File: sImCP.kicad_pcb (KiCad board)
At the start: 2 copper layers, 155.6 x 140 mm, 79 parts, among them J1 AVR-ISP-6, SW1 RESET, SW2 BOOT, U1 ATmega328P-AU, Y1 16MHz

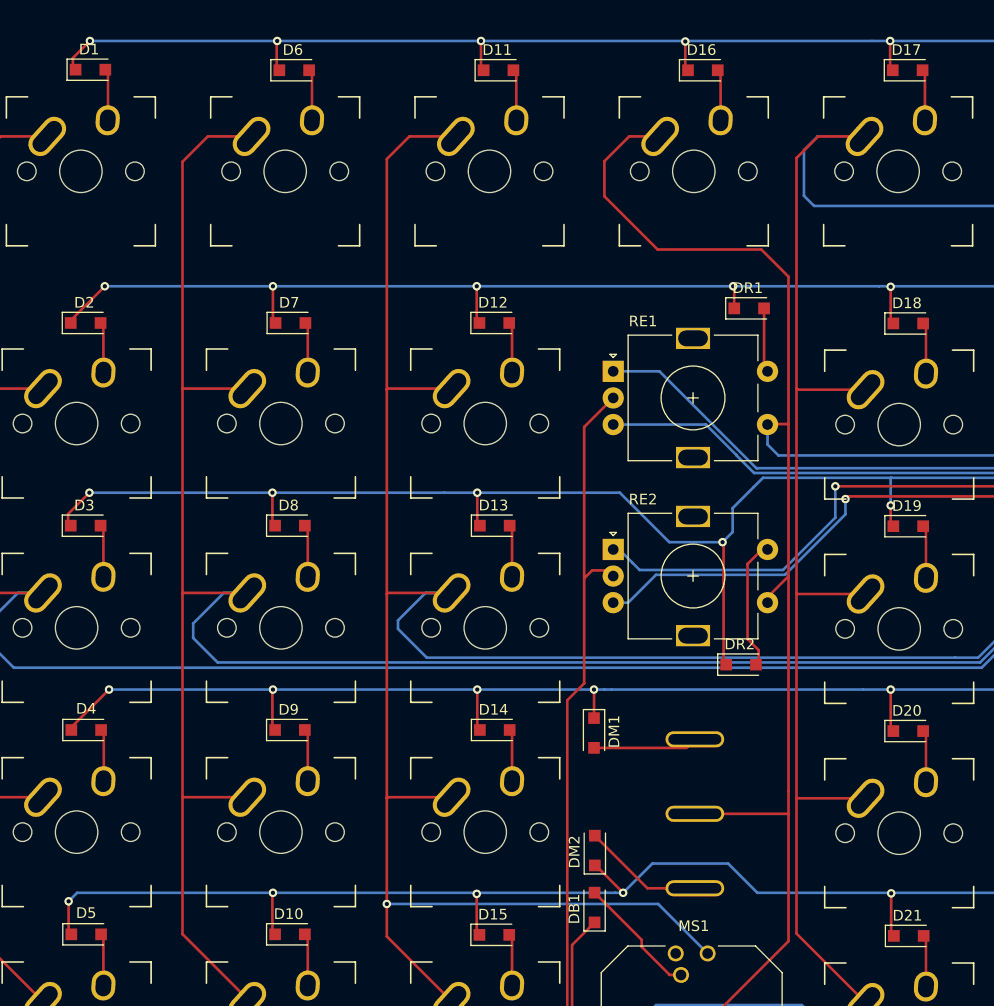
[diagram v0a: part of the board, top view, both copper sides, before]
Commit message: update diode footprint to SOD-123FL
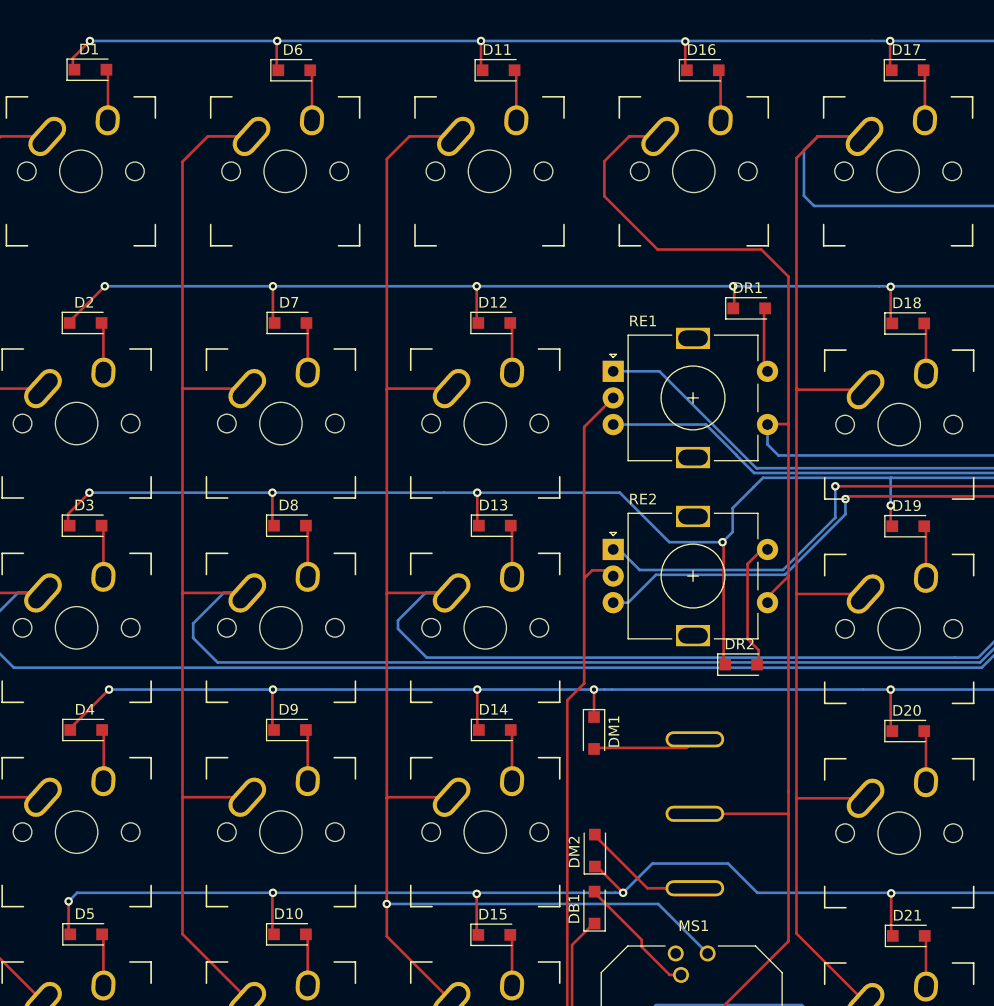
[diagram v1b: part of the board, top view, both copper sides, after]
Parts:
- D1, D10, D11, D12, D13, D14, D15, D16, D17, D18, D19, D2, D20, D21, D3, D4, D5, D6, D7, D8, D9, DB1, DM1, DM2, DR1, DR2: footprint Diode_SMD:D_SOD-123F -> SOD-123FL:D_SOD-123FL
